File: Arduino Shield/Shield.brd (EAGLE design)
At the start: 117.2 x 100 mm, 33 parts, among them IC1 317T, IC2 317T

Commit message: Конечная разводка
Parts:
- moved R2 7.51 mm to (78.8, 57.3)
- moved R5 7.50 mm to (74.8, 57.4)
- moved R8 4.80 mm to (52.6, 45.1)
- moved R10 3.90 mm to (53.3, 30.8)
- moved C2 2.76 mm to (61.7, 29.6)
- moved C5 2.22 mm to (61.8, 40.7)
- moved R9 1.36 mm to (55.7, 35.2), turned to 270 degrees
- moved C1 1.13 mm to (55.7, 40.7), turned to 90 degrees
- moved C4 1.02 mm to (61.8, 51.0)
- moved R7 0.63 mm to (56.7, 48.9)
- moved C3 0.60 mm to (56.8, 53.1)
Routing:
- net SD_CS: track 25.8 -> 16.5 mm
- net PIN4: track 8.09 -> 15.1 mm
- net GND: track 419.2 -> 423.2 mm, vias 1 -> 3
- net 3.3V: track 36.4 -> 39.9 mm
- net SD_DI: track 19.0 -> 16.4 mm
- net V_IN: track 167.4 -> 165.8 mm
- net PIN12: track 52.9 -> 51.9 mm
- net N$2: track 9.11 -> 8.27 mm
- net 6V: track 82.0 -> 82.7 mm
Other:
- board size 117.2 x 100 mm -> 69.2 x 56.6 mm

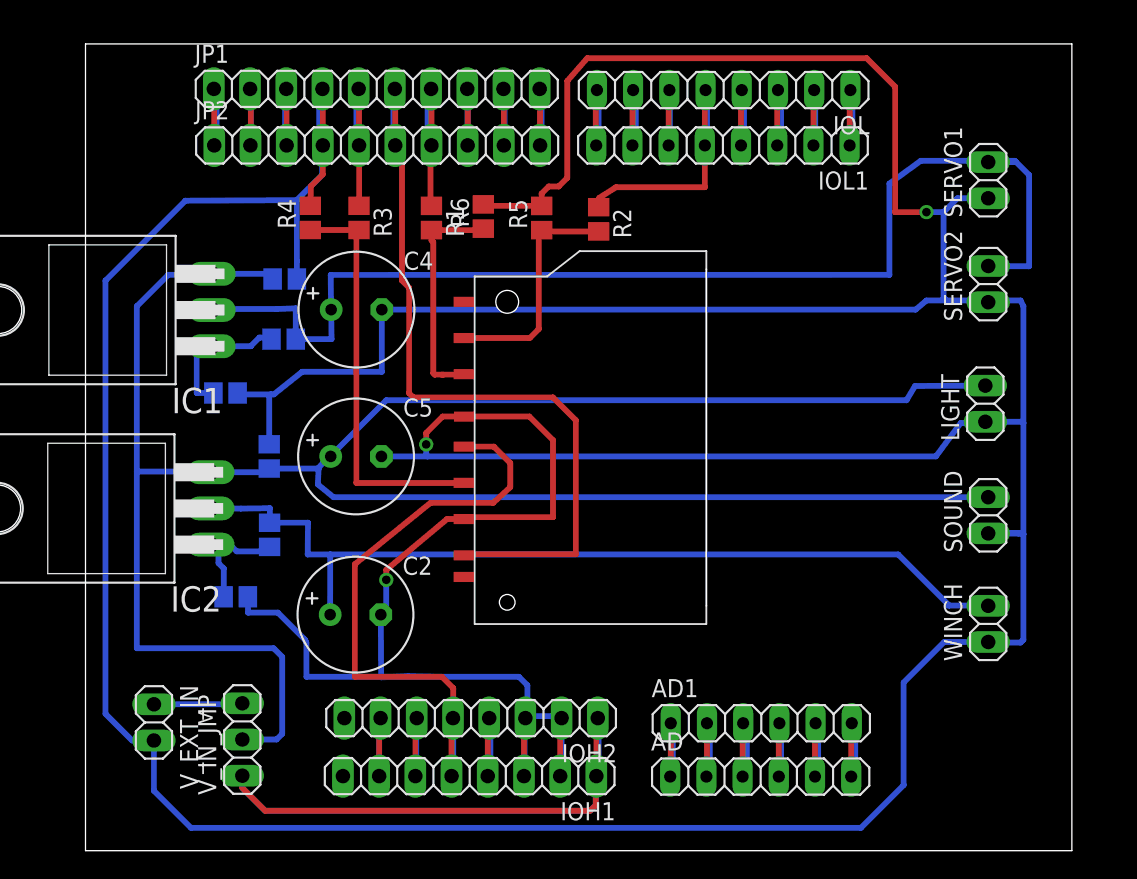
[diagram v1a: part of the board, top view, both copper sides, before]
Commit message: Больше места под sd
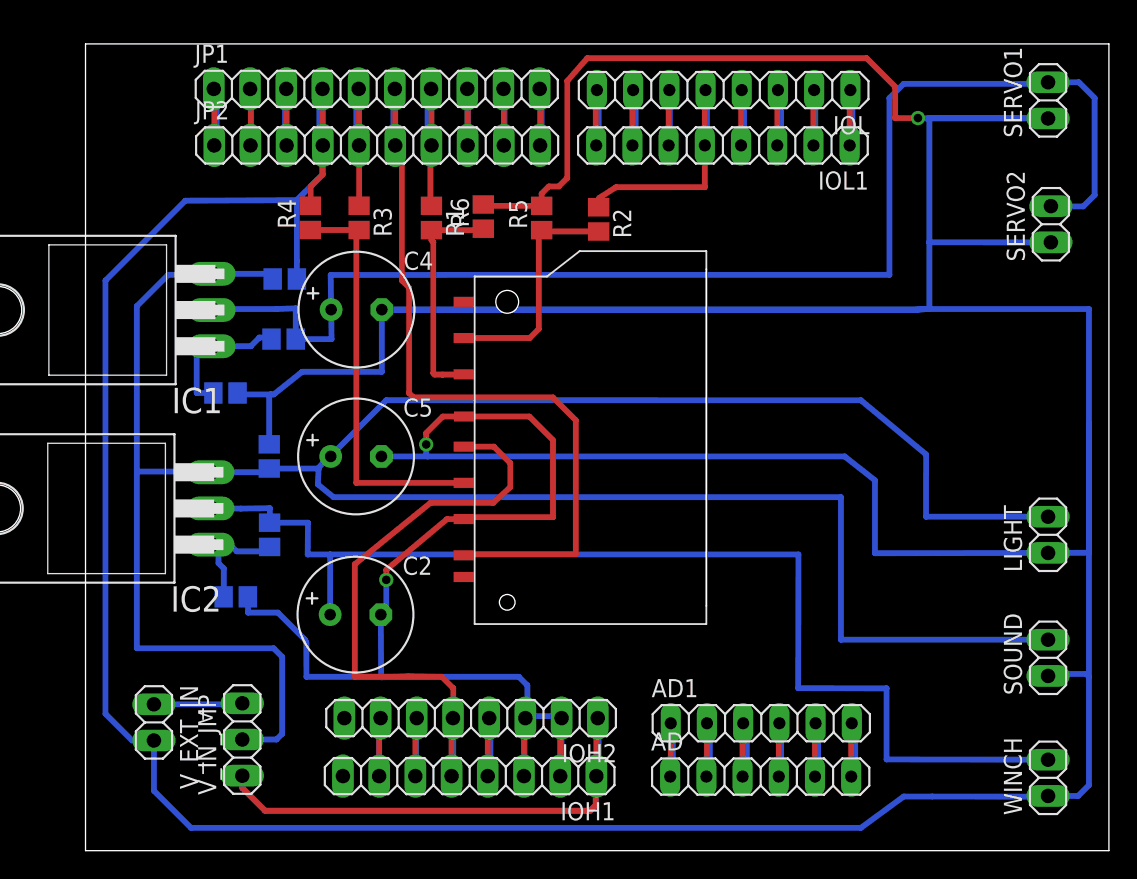
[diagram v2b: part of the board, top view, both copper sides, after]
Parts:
- moved WINCH 11.6 mm to (110.3, 18.1)
- moved SOUND 10.8 mm to (110.3, 26.5)
- moved LIGHT 10.2 mm to (110.3, 35.2)
- moved SERVO1 7.00 mm to (110.3, 65.6)
- moved SERVO2 6.08 mm to (110.5, 57.0)
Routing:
- net GND: track 423.2 -> 509.1 mm
- net V_IN: track 165.8 -> 189.5 mm
- net 7V: track 63.8 -> 80.7 mm
- net 6V: track 82.7 -> 92.4 mm
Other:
- board size 69.2 x 56.6 mm -> 71.8 x 56.6 mm
